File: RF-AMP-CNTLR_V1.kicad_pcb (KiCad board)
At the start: 4 copper layers, 220 x 100 mm, 384 parts, among them J101 VAC, J102 VDC, J103 ext_13V8, J104 Front Panel, J105 ANT_SWITCH, J106 BAND_SELECT, J107 I2C0, J108 VDD_IN, J109 VSS_IN, J110 RELAY RF OUT, J111 RELAY RF IN, J112 FWD3, J113 REF3, J114 FWD4, J115 REF4, J116 PTT, J117 ALC, J118 VDD_AMP, J119 GND_AMP, J120 SPI0, J121 I2C1, J122 RS232, J123 AMP1, J124 AMP2, J201 Raspberry_Pi_2_3, Q101 DTA124E, Q201 BSS138, Q202 BSS138, Q301 BC857, Q302 BC857, Q303 BC857, Q304 BC857, Q305 BC857, Q306 BC857, Q307 BC857, Q308 BC857, Q309 BC857, Q310 BC857, Q311 BC857, Q312 BC857, Q313 DTC124E, Q314 DTC124E, Q315 DTC124E, Q316 DTC124E, Q317 BC857, Q318 BC857, Q319 BC857, Q320 BC857, Q321 DTA124E, Q322 DTA124E, Q323 BC857, Q324 BC857, Q325 DTC124E, Q326 DTC124E, Q327 DTC124E, Q328 DTC124E, Q329 DTC124E, Q330 DTC124E, Q331 DTC124E, Q332 DTA124E, Q401 IXTH140P10T, Q402 IXTH140P10T, Q403 DTC124E, Q404 BC857, Q405 DTC124E, Q406 DTC124E, Q407 DTC124E, Q408 DTA124E, Q409 DTC124E, Q410 DTC124E, Q411 DTA124E, Q412 BCX53, Q413 DTA124E, Q414 DTC124E, Q415 DTC124E, Q416 BCX53, Q417 DTA124E, Q418 DTC124E, Q419 DTC124E, Q420 BCX53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

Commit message: Review
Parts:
- C102, C103: value 470n -> 68n
- C104, C110, C111, C112, C113, C120, C121, C122: value 100u -> 47u
- C108, C109: value 470n -> 47n
- C202: value 10u -> 47u
- D305, D306, D307, D308, D314, D315, D316, D317, D319, D404, D406, D409, D410, D413, D414: value DZ2S047X0L -> BZT52C4V7T-7
- D402: value DZ2S130X0L -> BZT52C13T-7
- D405: value DZ2S030X0L -> BZT52C13T-7
- F101, F102: value 0.1AT -> 1AT
- R406: value 10k -> 6k8
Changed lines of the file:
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@@
       (effects (font (size 1 1) (thickness 0.15)))
     )
-    (fp_text value 470n (at 5 3.25) (layer F.Fab)
+    (fp_text value 68n (at 5 3.25) (layer F.Fab)
       (effects (font (size 1 1) (thickness 0.15)))
     )
@@
       (effects (font (size 1 1) (thickness 0.15)))
     )
-    (fp_text value 470n (at 5 3.25) (layer F.Fab)
+    (fp_text value 68n (at 5 3.25) (layer F.Fab)
       (effects (font (size 1 1) (thickness 0.15)))
     )
@@
       (effects (font (size 1 1) (thickness 0.15)))
     )
-    (fp_text value 0.1AT (at 2.54 5 90) (layer F.Fab)
+    (fp_text value 1AT (at 2.54 5 90) (layer F.Fab)
       (effects (font (size 1 1) (thickness 0.15)))
     )
@@
       (effects (font (size 1 1) (thickness 0.15)))
     )
-    (fp_text value 0.1AT (at 2.54 5 90) (layer F.Fab)
+    (fp_text value 1AT (at 2.54 5 90) (layer F.Fab)
       (effects (font (size 1 1) (thickness 0.15)))
     )
@@
       (effects (font (size 1 1) (thickness 0.15)))
     )
-    (fp_text value 470n (at 2.5 3 90) (layer F.Fab)
+    (fp_text value 47n (at 2.5 3 90) (layer F.Fab)
       (effects (font (size 1 1) (thickness 0.15)))
     )
@@
       (effects (font (size 1 1) (thickness 0.15)))
     )
-    (fp_text value 470n (at 2.5 3 90) (layer F.Fab)
+    (fp_text value 47n (at 2.5 3 90) (layer F.Fab)
       (effects (font (size 1 1) (thickness 0.15)))
     )
@@
       (effects (font (size 1 1) (thickness 0.15)) (justify mirror))
     )
-    (fp_text value 100u (at 0 -2.55 90) (layer B.Fab)
+    (fp_text value 47u (at 0 -2.55 90) (layer B.Fab)
       (effects (font (size 1 1) (thickness 0.15)) (justify mirror))
     )
@@
       (effects (font (size 1 1) (thickness 0.15)) (justify mirror))
     )
-    (fp_text value 100u (at 0 -2.55 90) (layer B.Fab)
+    (fp_text value 47u (at 0 -2.55 90) (layer B.Fab)
       (effects (font (size 1 1) (thickness 0.15)) (justify mirror))
     )
@@
       (effects (font (size 1 1) (thickness 0.15)) (justify mirror))
     )
-    (fp_text value 100u (at 0 -2.55 270) (layer B.Fab)
+    (fp_text value 47u (at 0 -2.55 270) (layer B.Fab)
       (effects (font (size 1 1) (thickness 0.15)) (justify mirror))
     )
@@
       (effects (font (size 1 1) (thickness 0.15)) (justify mirror))
     )
-    (fp_text value 100u (at 0 -2.55 90) (layer B.Fab)
+    (fp_text value 47u (at 0 -2.55 90) (layer B.Fab)
       (effects (font (size 1 1) (thickness 0.15)) (justify mirror))
     )
@@
       (effects (font (size 1 1) (thickness 0.15)) (justify mirror))
     )
-    (fp_text value 100u (at 0 -2.55 90) (layer B.Fab)
+    (fp_text value 47u (at 0 -2.55 90) (layer B.Fab)
       (effects (font (size 1 1) (thickness 0.15)) (justify mirror))
     )
@@
       (effects (font (size 1 1) (thickness 0.15)) (justify mirror))
     )
-    (fp_text value 100u (at 0 -2.55 270) (layer B.Fab)
+    (fp_text value 47u (at 0 -2.55 270) (layer B.Fab)
       (effects (font (size 1 1) (thickness 0.15)) (justify mirror))
     )
@@
       (effects (font (size 1 1) (thickness 0.15)) (justify mirror))
     )
-    (fp_text value 100u (at 0 -2.55 90) (layer B.Fab)
+    (fp_text value 47u (at 0 -2.55 90) (layer B.Fab)
       (effects (font (size 1 1) (thickness 0.15)) (justify mirror))
     )
@@
       (effects (font (size 1 1) (thickness 0.15)) (justify mirror))
     )
-    (fp_text value 100u (at 0 -2.55 90) (layer B.Fab)
+    (fp_text value 47u (at 0 -2.55 90) (layer B.Fab)
       (effects (font (size 1 1) (thickness 0.15)) (justify mirror))
     )
@@
       (effects (font (size 1 1) (thickness 0.15)))
     )
-    (fp_text value 10u (at 0 2.55 270) (layer F.Fab)
+    (fp_text value 47u (at 0 2.55 270) (layer F.Fab)
       (effects (font (size 1 1) (thickness 0.15)))
     )
@@
       (effects (font (size 1 1) (thickness 0.15)) (justify mirror))
     )
-    (fp_text value DZ2S047X0L (at 0 -1.4) (layer B.Fab)
+    (fp_text value BZT52C4V7T-7 (at 0 -1.4) (layer B.Fab)
       (effects (font (size 1 1) (thickness 0.15)) (justify mirror))
     )
@@
       (effects (font (size 1 1) (thickness 0.15)) (justify mirror))
     )
-    (fp_text value DZ2S047X0L (at 0 -1.4) (layer B.Fab)
+    (fp_text value BZT52C4V7T-7 (at 0 -1.4) (layer B.Fab)
       (effects (font (size 1 1) (thickness 0.15)) (justify mirror))
     )
@@
       (effects (font (size 1 1) (thickness 0.15)) (justify mirror))
     )
-    (fp_text value DZ2S047X0L (at 0 -1.4 90) (layer B.Fab)
+    (fp_text value BZT52C4V7T-7 (at 0 -1.4 90) (layer B.Fab)
       (effects (font (size 1 1) (thickness 0.15)) (justify mirror))
     )
@@
       (effects (font (size 1 1) (thickness 0.15)) (justify mirror))
     )
-    (fp_text value DZ2S047X0L (at 0 -1.4) (layer B.Fab)
+    (fp_text value BZT52C4V7T-7 (at 0 -1.4) (layer B.Fab)
       (effects (font (size 1 1) (thickness 0.15)) (justify mirror))
     )
@@
       (effects (font (size 1 1) (thickness 0.15)))
     )
-    (fp_text value DZ2S047X0L (at 0 1.4) (layer F.Fab)
+    (fp_text value BZT52C4V7T-7 (at 0 1.4) (layer F.Fab)
       (effects (font (size 1 1) (thickness 0.15)))
     )
@@
       (effects (font (size 1 1) (thickness 0.15)))
     )
-    (fp_text value DZ2S047X0L (at 0 1.4) (layer F.Fab)
+    (fp_text value BZT52C4V7T-7 (at 0 1.4) (layer F.Fab)
       (effects (font (size 1 1) (thickness 0.15)))
     )
@@
       (effects (font (size 1 1) (thickness 0.15)))
     )
-    (fp_text value DZ2S047X0L (at 0 1.4) (layer F.Fab)
+    (fp_text value BZT52C4V7T-7 (at 0 1.4) (layer F.Fab)
       (effects (font (size 1 1) (thickness 0.15)))
     )
@@
       (effects (font (size 1 1) (thickness 0.15)))
     )
-    (fp_text value DZ2S047X0L (at 0 1.4) (layer F.Fab)
+    (fp_text value BZT52C4V7T-7 (at 0 1.4) (layer F.Fab)
       (effects (font (size 1 1) (thickness 0.15)))
     )
@@
       (effects (font (size 1 1) (thickness 0.15)))
     )
-    (fp_text value DZ2S047X0L (at 0 1.4 90) (layer F.Fab)
+    (fp_text value BZT52C4V7T-7 (at 0 1.4 90) (layer F.Fab)
       (effects (font (size 1 1) (thickness 0.15)))
     )
@@
       (effects (font (size 1 1) (thickness 0.15)))
     )
-    (fp_text value DZ2S130X0L (at 0 1.4 180) (layer F.Fab)
+    (fp_text value BZT52C13T-7 (at 0 1.4 180) (layer F.Fab)
       (effects (font (size 1 1) (thickness 0.15)))
     )
@@
       (effects (font (size 1 1) (thickness 0.15)))
     )
-    (fp_text value DZ2S047X0L (at 0 1.4 90) (layer F.Fab)
+    (fp_text value BZT52C4V7T-7 (at 0 1.4 90) (layer F.Fab)
       (effects (font (size 1 1) (thickness 0.15)))
     )
@@
       (effects (font (size 1 1) (thickness 0.15)))
     )
-    (fp_text value DZ2S030X0L (at 0 1.4 180) (layer F.Fab)
+    (fp_text value BZT52C13T-7 (at 0 1.4 180) (layer F.Fab)
       (effects (font (size 1 1) (thickness 0.15)))
     )
@@
       (effects (font (size 1 1) (thickness 0.15)))
     )
-    (fp_text value DZ2S047X0L (at 0 1.4 90) (layer F.Fab)
+    (fp_text value BZT52C4V7T-7 (at 0 1.4 90) (layer F.Fab)
       (effects (font (size 1 1) (thickness 0.15)))
     )
@@
       (effects (font (size 1 1) (thickness 0.15)))
     )
-    (fp_text value DZ2S047X0L (at 0 1.4) (layer F.Fab)
+    (fp_text value BZT52C4V7T-7 (at 0 1.4) (layer F.Fab)
       (effects (font (size 1 1) (thickness 0.15)))
     )
@@
       (effects (font (size 1 1) (thickness 0.15)))
     )
-    (fp_text value DZ2S047X0L (at 0 1.4) (layer F.Fab)
+    (fp_text value BZT52C4V7T-7 (at 0 1.4) (layer F.Fab)
       (effects (font (size 1 1) (thickness 0.15)))
     )
@@
       (effects (font (size 1 1) (thickness 0.15)))
     )
-    (fp_text value DZ2S047X0L (at 0 1.4 270) (layer F.Fab)
+    (fp_text value BZT52C4V7T-7 (at 0 1.4 270) (layer F.Fab)
       (effects (font (size 1 1) (thickness 0.15)))
     )
@@
       (effects (font (size 1 1) (thickness 0.15)))
     )
-    (fp_text value DZ2S047X0L (at 0 1.4) (layer F.Fab)
+    (fp_text value BZT52C4V7T-7 (at 0 1.4) (layer F.Fab)
       (effects (font (size 1 1) (thickness 0.15)))
     )
@@
       (effects (font (size 1 1) (thickness 0.15)) (justify mirror))
     )
-    (fp_text value 10k (at 0 -1.65) (layer B.Fab)
+    (fp_text value 6k8 (at 0 -1.65) (layer B.Fab)
       (effects (font (size 1 1) (thickness 0.15)) (justify mirror))
     )

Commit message: prototype bug fixes
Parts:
- C204: moved to B.Cu
- moved C204 40.6 mm to (104.6, 128.2), turned to 270 degrees
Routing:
- net Earth: track 213.5 -> 209.2 mm
- net Net-(C102-Pad1): track 43.0 -> 44.1 mm
- net Net-(C103-Pad2): track 108.5 -> 109.6 mm
- net Net-(C103-Pad1): track 94.7 -> 95.7 mm
- net Net-(C102-Pad2): track 34.8 -> 35.9 mm
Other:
- net class Vdd: clearance 1 -> 0.3
- board text added: "HB9GKW RF-AMP-CNTLR_V1"
- board text removed: "HB9GKW PA_CNTLR_V1"

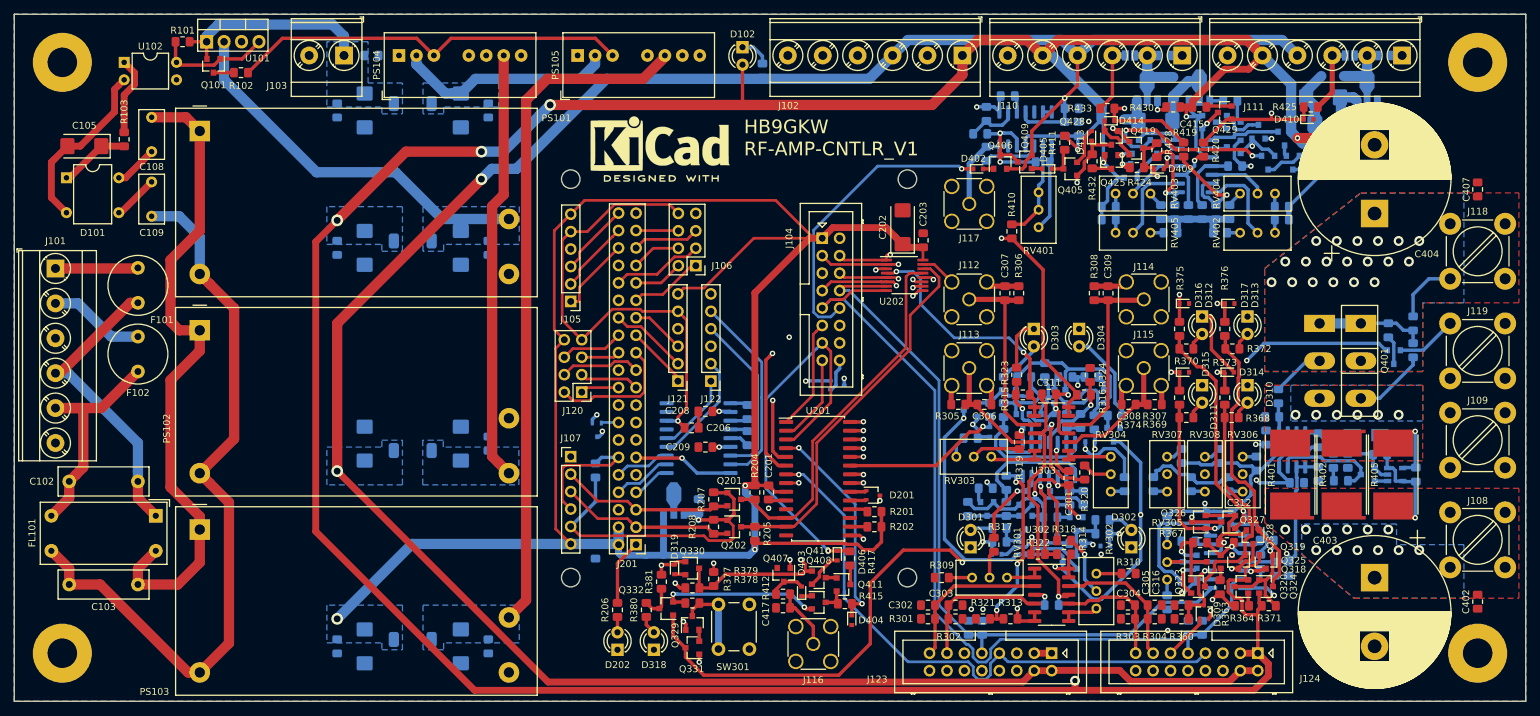
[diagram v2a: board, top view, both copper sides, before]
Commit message: new Version with AVR Controller
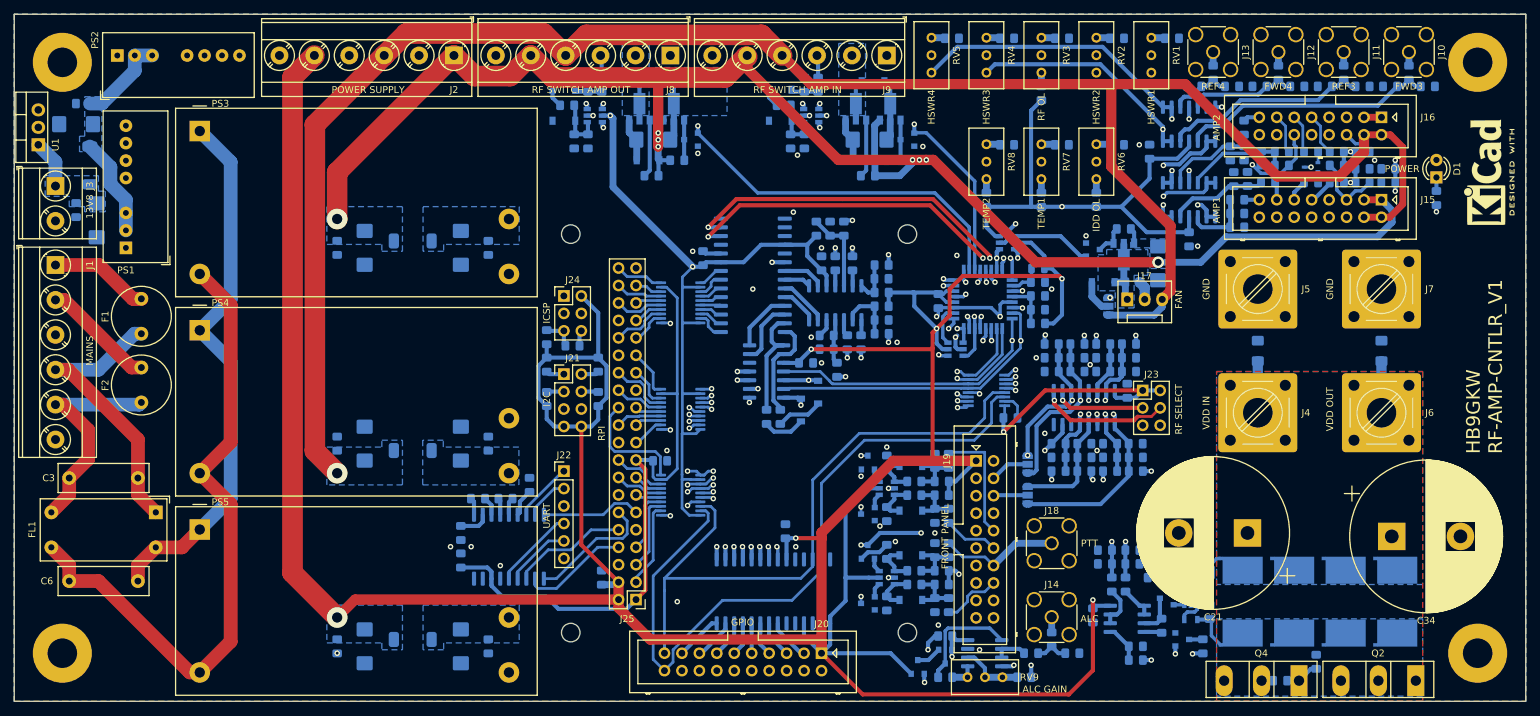
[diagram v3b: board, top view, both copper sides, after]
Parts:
- removed C101, C123, C201, C203, C204, C205, C206, C207, C208, C209, C301, C310, C311, C312, C401, C402, C405, C406, C407, C408, C409, C410, C411, C412, C413, C414, C415, C416, C417, C418, C419, C423, C427: 100n, Capacitor_SMD:C_0805_2012Metric_Pad1.15x1.40mm_HandSolder
- removed C105, C202: 47u, Capacitor_Tantalum_SMD:CP_EIA-6032-28_Kemet-C
- removed C108, C109: 47n, Capacitor_THT:C_Rect_L7.0mm_W3.5mm_P5.00mm
- removed C302, C303, C304, C305, C306, C307, C308, C309, C313, C314, C315, C316: 47n, Capacitor_SMD:C_0805_2012Metric_Pad1.15x1.40mm_HandSolder
- removed C403, C404: 470u, Capacitor_THT:CP_Radial_D22.0mm_P10.00mm_SnapIn
- removed C420, C421, C424, C425: 1u, Capacitor_SMD:C_0805_2012Metric_Pad1.15x1.40mm_HandSolder
- removed C422, C426: 4u7, Capacitor_Tantalum_SMD:CP_EIA-6032-28_Kemet-C
- removed D101: B80C800DM, Diode_THT:Diode_Bridge_DIP-4_W7.62mm_P5.08mm
- removed D103, D104, D309: BAT54CW, Package_TO_SOT_SMD:SOT-323_SC-70
- removed D201: BAT54AW, Package_TO_SOT_SMD:SOT-323_SC-70
- removed D202: RP_ON, LED_THT:LED_D3.0mm
- removed D301: HSWR1, LED_THT:LED_D3.0mm
- removed D302: HSWR2, LED_THT:LED_D3.0mm
- removed D303: HSWR3, LED_THT:LED_D3.0mm
- removed D304: HSWR4, LED_THT:LED_D3.0mm
- removed D305, D306, D307, D308, D314, D315, D316, D317, D319, D404, D406, D409, D410, D413, D414: BZT52C4V7T-7, Diode_SMD:D_SOD-523
- removed D310: RF_OL, LED_THT:LED_D3.0mm
- removed D311: TEMP1, LED_THT:LED_D3.0mm
- removed D312: TEMP2, LED_THT:LED_D3.0mm
- removed D313: OC, LED_THT:LED_D3.0mm
- removed D318: FAULT, LED_THT:LED_D3.0mm
- removed D401: Z1SMA33, Diode_SMD:D_SMA
- removed D402, D405: BZT52C13T-7, Diode_SMD:D_SOD-523
- removed D403: DZ2S047X0L, Diode_SMD:D_SOD-523
- removed D407, D408, D411, D412: PMEG6010CEH, Diode_SMD:D_SOD-123
- removed J104: Front Panel, Connector_Multicomp:Multicomp_MC9A12-1634_2x08_P2.54mm_Vertical
- removed J105: ANT_SWITCH, Connector_PinHeader_2.54mm:PinHeader_1x06_P2.54mm_Vertical
- removed J106: BAND_SELECT, Connector_PinHeader_2.54mm:PinHeader_2x04_P2.54mm_Vertical
- removed J107: I2C0, Connector_PinHeader_2.54mm:PinHeader_1x06_P2.54mm_Vertical
- removed J108: VDD_IN, TerminalBlock_MetzConnect:TerminalBlock_MetzConnect_360425_1x01_Horizontal_ScrewM4.0_Boxed
- removed J109: VSS_IN, TerminalBlock_MetzConnect:TerminalBlock_MetzConnect_360425_1x01_Horizontal_ScrewM4.0_Boxed
- removed J112: FWD3, Connector_Coaxial:SMA_Amphenol_132134_Vertical
- removed J113: REF3, Connector_Coaxial:SMA_Amphenol_132134_Vertical
- removed J114: FWD4, Connector_Coaxial:SMA_Amphenol_132134_Vertical
- removed J115: REF4, Connector_Coaxial:SMA_Amphenol_132134_Vertical
- removed J116: PTT, Connector_Coaxial:SMA_Amphenol_132134_Vertical
- removed J117: ALC, Connector_Coaxial:SMA_Amphenol_132134_Vertical
- removed J118: VDD_AMP, TerminalBlock_MetzConnect:TerminalBlock_MetzConnect_360425_1x01_Horizontal_ScrewM4.0_Boxed
- removed J119: GND_AMP, TerminalBlock_MetzConnect:TerminalBlock_MetzConnect_360425_1x01_Horizontal_ScrewM4.0_Boxed
- removed J120: SPI0, Connector_PinHeader_2.54mm:PinHeader_2x04_P2.54mm_Vertical
- removed J121: I2C1, Connector_PinHeader_2.54mm:PinHeader_1x06_P2.54mm_Vertical
- removed J122: RS232, Connector_PinHeader_2.54mm:PinHeader_1x06_P2.54mm_Vertical
- removed J123: AMP1, Connector_Multicomp:Multicomp_MC9A12-1634_2x08_P2.54mm_Vertical
- removed J124: AMP2, Connector_Multicomp:Multicomp_MC9A12-1634_2x08_P2.54mm_Vertical
- removed JP401, JP402: SolderJumper_2_Open, Jumper:SolderJumper-2_P1.3mm_Open_Pad1.0x1.5mm
- removed Q101, Q321, Q322, Q332, Q408, Q411, Q413, Q417, Q421, Q425: DTA124E, Package_TO_SOT_SMD:SOT-23
- removed Q201, Q202: BSS138, Package_TO_SOT_SMD:SOT-23
- removed Q301, Q302, Q303, Q304, Q305, Q306, Q307, Q308, Q309, Q310, Q311, Q312, Q317, Q318, Q319, Q320, Q323, Q324, Q404: BC857, Package_TO_SOT_SMD:SOT-23
- removed Q313, Q314, Q315, Q316, Q325, Q326, Q327, Q328, Q329, Q330, Q331, Q403, Q405, Q406, Q407, Q409, Q410, Q414, Q415, Q418, Q419, Q422, Q423, Q424, Q427, Q428, Q429: DTC124E, Package_TO_SOT_SMD:SOT-23
- removed Q401, Q402: IXTH140P10T, Package_TO_SOT_THT:TO-247-3_Vertical
- removed Q412, Q416, Q420, Q426: BCX53, Package_TO_SOT_SMD:SOT-89-3
- removed R101, R325, R326, R327, R328, R333, R334, R335, R336, R363, R364, R365, R366, R378: 22k, Resistor_SMD:R_0805_2012Metric_Pad1.15x1.40mm_HandSolder
- removed R102, R377, R412, R415, R417, R424, R425, R432, R433, R434, R435, R436, R437: 1k, Resistor_SMD:R_0805_2012Metric_Pad1.15x1.40mm_HandSolder
- removed R103: 620, Resistor_SMD:R_0805_2012Metric_Pad1.15x1.40mm_HandSolder
- removed R104, R201, R202: 2k2, Resistor_SMD:R_0805_2012Metric_Pad1.15x1.40mm_HandSolder
- removed R203: 1k5, Resistor_SMD:R_0805_2012Metric_Pad1.15x1.40mm_HandSolder
- removed R204, R205, R206: 2k7, Resistor_SMD:R_0805_2012Metric_Pad1.15x1.40mm_HandSolder
- removed R207, R208: 1k8, Resistor_SMD:R_0805_2012Metric_Pad1.15x1.40mm_HandSolder
- removed R301, R302, R303, R304, R305, R306, R307, R308, R353, R356, R359, R360, R361, R362, R403, R409, R414: 100k, Resistor_SMD:R_0805_2012Metric_Pad1.15x1.40mm_HandSolder
- removed R309, R310, R311, R312, R350, R352: 15k, Resistor_SMD:R_0805_2012Metric_Pad1.15x1.40mm_HandSolder
- removed R313, R314, R315, R316: 82k, Resistor_SMD:R_0805_2012Metric_Pad1.15x1.40mm_HandSolder
- removed R317, R318, R319, R320, R349, R351, R354, R357, R379, R411, R418, R421, R426, R429: 47k, Resistor_SMD:R_0805_2012Metric_Pad1.15x1.40mm_HandSolder
- removed R321, R322, R323, R324, R337, R339, R341, R343, R355, R358, R367, R371, R404, R410, R413, R419, R420, R422, R423, R427, R428, R430, R431: 10k, Resistor_SMD:R_0805_2012Metric_Pad1.15x1.40mm_HandSolder
- removed R329, R330, R331, R332: 820k, Resistor_SMD:R_0805_2012Metric_Pad1.15x1.40mm_HandSolder
- removed R338, R340, R342, R344, R368, R369, R370, R372, R380, R407: 4k7, Resistor_SMD:R_0805_2012Metric_Pad1.15x1.40mm_HandSolder
- removed R345, R346, R347, R348, R373, R374, R375, R376, R381: 470, Resistor_SMD:R_0805_2012Metric_Pad1.15x1.40mm_HandSolder
- removed R401, R402, R405: 0R015, Resistor_SMD:R_Shunt_Vishay_WSR2_WSR3_KelvinConnection
- removed R406: 6k8, Resistor_SMD:R_0805_2012Metric_Pad1.15x1.40mm_HandSolder
- removed R408: 68k, Resistor_SMD:R_0805_2012Metric_Pad1.15x1.40mm_HandSolder
- removed R416: 33k, Resistor_SMD:R_0805_2012Metric_Pad1.15x1.40mm_HandSolder
- removed the REF** at (114.0, 68.8)
- removed RV301, RV302, RV303, RV304, RV305, RV306, RV307, RV308: 50k, Potentiometer_THT:Potentiometer_Bourns_3296W_Vertical
- removed RV401, RV402, RV403, RV404, RV405: 20k, Potentiometer_THT:Potentiometer_Bourns_3296W_Vertical
- removed SW301: RESET, Button_Switch_THT:SW_PUSH_6mm
- removed U101: KA378R12C, Package_TO_SOT_THT:TO-220-4_Vertical
- removed U102: SFH617A-2, Package_DIP:DIP-4_W7.62mm
- removed U103: L78L33_SOT89, Package_TO_SOT_SMD:SOT-89-3
- removed U201: MCP23017_SO, Package_SO:SOIC-28W_7.5x17.9mm_P1.27mm
- removed U202: MAX11616, Package_SO:QSOP-16_3.9x4.9mm_P0.635mm
- removed U203: MAX3232, Package_SO:SOIC-18W_7.5x11.6mm_P1.27mm
- removed U301, U304, U404: LM339, Package_SO:SOIC-14_3.9x8.7mm_P1.27mm
- removed U302, U303, U402: MC33079, Package_SO:SOIC-14_3.9x8.7mm_P1.27mm
- removed U401: MC33078, Package_SO:SOIC-8_3.9x4.9mm_P1.27mm
- removed U403: INA138, Package_TO_SOT_SMD:SOT-23-5
- added C19: 100n, Capacitor_SMD:C_0805_2012Metric_Pad1.15x1.40mm_HandSolder, B.Cu at (177.0, 137.5)
- added C20: 100n, Capacitor_SMD:C_1206_3216Metric_Pad1.42x1.75mm_HandSolder, B.Cu at (201.0, 99.0)
- added C21: 470u, Capacitor_THT:CP_Radial_D22.0mm_P10.00mm_SnapIn, F.Cu at (199.5, 125.5)
- added C22: 47n, Capacitor_SMD:C_0805_2012Metric_Pad1.15x1.40mm_HandSolder, B.Cu at (199.5, 74.0)
- added C23: 47n, Capacitor_SMD:C_0805_2012Metric_Pad1.15x1.40mm_HandSolder, B.Cu at (198.0, 79.0)
- added C24: 47n, Capacitor_SMD:C_0805_2012Metric_Pad1.15x1.40mm_HandSolder, B.Cu at (201.5, 71.0)
- added C25: 47n, Capacitor_SMD:C_0805_2012Metric_Pad1.15x1.40mm_HandSolder, B.Cu at (199.0, 70.2)
- added C26: 100n, Capacitor_SMD:C_0805_2012Metric_Pad1.15x1.40mm_HandSolder, B.Cu at (194.0, 137.0)
- added C27: 47n, Capacitor_SMD:C_0805_2012Metric_Pad1.15x1.40mm_HandSolder, B.Cu at (174.8, 100.0)
- added C28: 47n, Capacitor_SMD:C_0805_2012Metric_Pad1.15x1.40mm_HandSolder, B.Cu at (183.2, 114.5)
- added C29: 47n, Capacitor_SMD:C_0805_2012Metric_Pad1.15x1.40mm_HandSolder, B.Cu at (178.5, 100.0)
- added C30: 47n, Capacitor_SMD:C_0805_2012Metric_Pad1.15x1.40mm_HandSolder, B.Cu at (172.0, 114.5)
- added C31: 100n, Capacitor_SMD:C_0805_2012Metric_Pad1.15x1.40mm_HandSolder, B.Cu at (192.2, 134.0)
- added C32: 100n, Capacitor_SMD:C_0805_2012Metric_Pad1.15x1.40mm_HandSolder, B.Cu at (182.8, 130.0)
- added C33: 100n, Capacitor_SMD:C_0805_2012Metric_Pad1.15x1.40mm_HandSolder, B.Cu at (204.2, 147.0)
- added C34: 470u, Capacitor_THT:CP_Radial_D22.0mm_P10.00mm_SnapIn, F.Cu at (220.5, 126.0)
- added C35: 100n, Capacitor_SMD:C_1206_3216Metric_Pad1.42x1.75mm_HandSolder, B.Cu at (219.0, 99.0)
- added C36: 100n, Capacitor_SMD:C_0805_2012Metric_Pad1.15x1.40mm_HandSolder, B.Cu at (178.8, 130.0)
- added C37: 47n, Capacitor_SMD:C_0805_2012Metric_Pad1.15x1.40mm_HandSolder, B.Cu at (220.2, 60.5)
- added C38: 47n, Capacitor_SMD:C_0805_2012Metric_Pad1.15x1.40mm_HandSolder, B.Cu at (210.8, 60.5)
- added C39: 47n, Capacitor_SMD:C_0805_2012Metric_Pad1.15x1.40mm_HandSolder, B.Cu at (201.2, 60.5)
- added C40: 47n, Capacitor_SMD:C_0805_2012Metric_Pad1.15x1.40mm_HandSolder, B.Cu at (191.8, 60.5)
- added C41: 47n, Capacitor_SMD:C_0805_2012Metric_Pad1.15x1.40mm_HandSolder, B.Cu at (182.2, 100.0)
- added C42: 47n, Capacitor_SMD:C_0805_2012Metric_Pad1.15x1.40mm_HandSolder, B.Cu at (179.5, 114.5)
- added C43: 47n, Capacitor_SMD:C_0805_2012Metric_Pad1.15x1.40mm_HandSolder, B.Cu at (171.0, 100.0)
- added C44: 47n, Capacitor_SMD:C_0805_2012Metric_Pad1.15x1.40mm_HandSolder, B.Cu at (175.8, 112.5)
- added C45: 100n, Capacitor_SMD:C_0805_2012Metric_Pad1.15x1.40mm_HandSolder, B.Cu at (155.5, 140.5)
- added C46: 47n, Capacitor_SMD:C_0805_2012Metric_Pad1.15x1.40mm_HandSolder, B.Cu at (216.2, 74.5)
- added C47: 47n, Capacitor_SMD:C_0805_2012Metric_Pad1.15x1.40mm_HandSolder, B.Cu at (216.2, 70.0)
- added C48: 47n, Capacitor_SMD:C_0805_2012Metric_Pad1.15x1.40mm_HandSolder, B.Cu at (220.0, 74.5)
- added C49: 100n, Capacitor_SMD:C_0805_2012Metric_Pad1.15x1.40mm_HandSolder, B.Cu at (174.0, 143.0)
- added C50: 100n, Capacitor_SMD:C_0805_2012Metric_Pad1.15x1.40mm_HandSolder, B.Cu at (137.5, 86.2)
- added C51: 100n, Capacitor_SMD:C_0805_2012Metric_Pad1.15x1.40mm_HandSolder, B.Cu at (191.0, 82.8)
- added C52: 100n, Capacitor_SMD:C_0805_2012Metric_Pad1.15x1.40mm_HandSolder, B.Cu at (135.2, 100.8)
- added C53: 100n, Capacitor_SMD:C_0805_2012Metric_Pad1.15x1.40mm_HandSolder, B.Cu at (185.2, 70.0)
- added C54: 4u7, Capacitor_Tantalum_SMD:CP_EIA-6032-28_Kemet-C, B.Cu at (113.0, 68.2)
- added C55: 4u7, Capacitor_Tantalum_SMD:CP_EIA-6032-28_Kemet-C, B.Cu at (144.5, 68.2)
- added C56: 47n, Capacitor_SMD:C_0805_2012Metric_Pad1.15x1.40mm_HandSolder, B.Cu at (103.5, 60.2)
- added C57: 47n, Capacitor_SMD:C_0805_2012Metric_Pad1.15x1.40mm_HandSolder, B.Cu at (103.5, 68.5)
- added C58: 47n, Capacitor_SMD:C_0805_2012Metric_Pad1.15x1.40mm_HandSolder, B.Cu at (135.0, 60.2)
- added C59: 47n, Capacitor_SMD:C_0805_2012Metric_Pad1.15x1.40mm_HandSolder, B.Cu at (133.0, 68.5)
- added C60: 1n, Capacitor_SMD:C_0805_2012Metric_Pad1.15x1.40mm_HandSolder, B.Cu at (154.0, 128.0)
- added C61: 1n, Capacitor_SMD:C_0805_2012Metric_Pad1.15x1.40mm_HandSolder, B.Cu at (154.0, 136.0)
- added C62: 1n, Capacitor_SMD:C_0805_2012Metric_Pad1.15x1.40mm_HandSolder, B.Cu at (154.0, 115.0)
- added C63: 1n, Capacitor_SMD:C_0805_2012Metric_Pad1.15x1.40mm_HandSolder, B.Cu at (154.0, 123.0)
- added C64: 100n, Capacitor_SMD:C_0805_2012Metric_Pad1.15x1.40mm_HandSolder, B.Cu at (182.0, 104.8)
- added C65: 100n, Capacitor_SMD:C_0805_2012Metric_Pad1.15x1.40mm_HandSolder, B.Cu at (147.0, 128.2)
- added C66: 100n, Capacitor_SMD:C_0805_2012Metric_Pad1.15x1.40mm_HandSolder, B.Cu at (147.0, 135.8)
- added C67: 100n, Capacitor_SMD:C_0805_2012Metric_Pad1.15x1.40mm_HandSolder, B.Cu at (147.0, 115.2)
- added C68: 100n, Capacitor_SMD:C_0805_2012Metric_Pad1.15x1.40mm_HandSolder, B.Cu at (147.0, 122.8)
- added C69: 1n, Capacitor_SMD:C_0805_2012Metric_Pad1.15x1.40mm_HandSolder, B.Cu at (101.2, 98.2)
- added C70: 100n, Capacitor_SMD:C_0805_2012Metric_Pad1.15x1.40mm_HandSolder, B.Cu at (169.0, 91.0)
- added C71: 100n, Capacitor_SMD:C_0805_2012Metric_Pad1.15x1.40mm_HandSolder, B.Cu at (154.5, 91.8)
- added C72: 100n, Capacitor_SMD:C_0805_2012Metric_Pad1.15x1.40mm_HandSolder, B.Cu at (169.0, 89.0)
- added C73: 1n, Capacitor_SMD:C_0805_2012Metric_Pad1.15x1.40mm_HandSolder, B.Cu at (182.8, 89.0)
- added C74: 47u, Capacitor_Tantalum_SMD:CP_EIA-6032-28_Kemet-C, B.Cu at (186.5, 86.2)
- added C75: 100n, Capacitor_SMD:C_0805_2012Metric_Pad1.15x1.40mm_HandSolder, B.Cu at (120.2, 85.5)
- added C76: 100n, Capacitor_SMD:C_0805_2012Metric_Pad1.15x1.40mm_HandSolder, B.Cu at (165.0, 108.8)
- added C77: 100n, Capacitor_SMD:C_0805_2012Metric_Pad1.15x1.40mm_HandSolder, B.Cu at (87.5, 120.5)
- added C78: 100n, Capacitor_SMD:C_0805_2012Metric_Pad1.15x1.40mm_HandSolder, B.Cu at (114.0, 115.0)
- added C79: 100n, Capacitor_SMD:C_0805_2012Metric_Pad1.15x1.40mm_HandSolder, B.Cu at (105.5, 132.0)
- added C80: 100n, Capacitor_SMD:C_0805_2012Metric_Pad1.15x1.40mm_HandSolder, B.Cu at (132.2, 125.2)
- added C81: 100n, Capacitor_SMD:C_0805_2012Metric_Pad1.15x1.40mm_HandSolder, B.Cu at (85.0, 129.5)
- added C82: 100n, Capacitor_SMD:C_0805_2012Metric_Pad1.15x1.40mm_HandSolder, B.Cu at (91.5, 120.5)
- added C83: 100n, Capacitor_SMD:C_0805_2012Metric_Pad1.15x1.40mm_HandSolder, B.Cu at (85.0, 125.5)
- added C84: 100n, Capacitor_SMD:C_0805_2012Metric_Pad1.15x1.40mm_HandSolder, B.Cu at (95.0, 118.5)
- added D10: 1N4148W, Diode_SMD:D_SOD-123, B.Cu at (100.0, 61.0)
- added D11: 1N4148W, Diode_SMD:D_SOD-123, B.Cu at (131.5, 61.0)
- added D12: PMEG6010CEH, Diode_SMD:D_SOD-123, B.Cu at (112.2, 71.2)
- added D13: PMEG6010CEH, Diode_SMD:D_SOD-123, B.Cu at (143.8, 71.2)
- added D14: 1N4148W, Diode_SMD:D_SOD-123, B.Cu at (150.5, 128.8)
- added D15: 1N4148W, Diode_SMD:D_SOD-123, B.Cu at (150.5, 135.2)
- added D16: 1N4148W, Diode_SMD:D_SOD-123, B.Cu at (150.5, 115.8)
- added D17: 1N4148W, Diode_SMD:D_SOD-123, B.Cu at (150.5, 122.2)
- added D18: PMEG6010CEH, Diode_SMD:D_SOD-123, B.Cu at (178.5, 89.0)
- added D2: Z1SMA33, Diode_SMD:D_SMA, B.Cu at (191.5, 131.2)
- added D3: 1N4148W, Diode_SMD:D_SOD-123, B.Cu at (134.5, 107.6)
- added D4: BAT54CW, Package_TO_SOT_SMD:SOT-323_SC-70, B.Cu at (208.8, 72.2)
- added D5: 1N4148W, Diode_SMD:D_SOD-123, B.Cu at (137.0, 105.0)
- added D6: PMEG6010CEH, Diode_SMD:D_SOD-123, B.Cu at (113.5, 59.8)
- added D7: BZT52C4V7T-7, Diode_SMD:D_SOD-123, B.Cu at (100.0, 65.5)
- added D8: PMEG6010CEH, Diode_SMD:D_SOD-123, B.Cu at (145.0, 59.8)
- added D9: BZT52C4V7T-7, Diode_SMD:D_SOD-123, B.Cu at (131.5, 65.5)
- added FB1: Ferrite_Bead_Small, Resistor_SMD:R_0805_2012Metric_Pad1.15x1.40mm_HandSolder, B.Cu at (202.5, 74.5)
- added FB10: Ferrite_Bead_Small, Resistor_SMD:R_0805_2012Metric_Pad1.15x1.40mm_HandSolder, B.Cu at (212.5, 70.0)
- added FB11: Ferrite_Bead_Small, Resistor_SMD:R_0805_2012Metric_Pad1.15x1.40mm_HandSolder, B.Cu at (208.8, 74.5)
- added FB12: Ferrite_Bead_Small, Resistor_SMD:R_0805_2012Metric_Pad1.15x1.40mm_HandSolder, B.Cu at (208.8, 70.0)
- added FB13: Ferrite_Bead_Small, Resistor_SMD:R_0805_2012Metric_Pad1.15x1.40mm_HandSolder, B.Cu at (171.0, 141.0)
- added FB14: Ferrite_Bead_Small, Resistor_SMD:R_0805_2012Metric_Pad1.15x1.40mm_HandSolder, B.Cu at (105.5, 60.2)
- added FB15: Ferrite_Bead_Small, Resistor_SMD:R_0805_2012Metric_Pad1.15x1.40mm_HandSolder, B.Cu at (137.0, 60.2)
- added FB16: Ferrite_Bead_Small, Resistor_SMD:R_0805_2012Metric_Pad1.15x1.40mm_HandSolder, B.Cu at (156.0, 128.0)
- added FB17: Ferrite_Bead_Small, Resistor_SMD:R_0805_2012Metric_Pad1.15x1.40mm_HandSolder, B.Cu at (156.0, 136.0)
- added FB18: Ferrite_Bead_Small, Resistor_SMD:R_0805_2012Metric_Pad1.15x1.40mm_HandSolder, B.Cu at (156.0, 115.0)
- added FB19: Ferrite_Bead_Small, Resistor_SMD:R_0805_2012Metric_Pad1.15x1.40mm_HandSolder, B.Cu at (156.0, 123.0)
- added FB2: Ferrite_Bead_Small, Resistor_SMD:R_0805_2012Metric_Pad1.15x1.40mm_HandSolder, B.Cu at (198.0, 77.0)
- added FB3: Ferrite_Bead_Small, Resistor_SMD:R_0805_2012Metric_Pad1.15x1.40mm_HandSolder, B.Cu at (204.5, 70.0)
- added FB4: Ferrite_Bead_Small, Resistor_SMD:R_0805_2012Metric_Pad1.15x1.40mm_HandSolder, B.Cu at (199.0, 66.5)
- added FB5: Ferrite_Bead_Small, Resistor_SMD:R_0805_2012Metric_Pad1.15x1.40mm_HandSolder, B.Cu at (223.0, 58.5)
- added FB6: Ferrite_Bead_Small, Resistor_SMD:R_0805_2012Metric_Pad1.15x1.40mm_HandSolder, B.Cu at (213.5, 58.5)
- added FB7: Ferrite_Bead_Small, Resistor_SMD:R_0805_2012Metric_Pad1.15x1.40mm_HandSolder, B.Cu at (204.0, 58.5)
- added FB8: Ferrite_Bead_Small, Resistor_SMD:R_0805_2012Metric_Pad1.15x1.40mm_HandSolder, B.Cu at (194.5, 58.5)
- added FB9: Ferrite_Bead_Small, Resistor_SMD:R_0805_2012Metric_Pad1.15x1.40mm_HandSolder, B.Cu at (212.5, 74.5)
- added J10: FWD3, Connector_Coaxial:SMA_Amphenol_132134_Vertical, F.Cu at (223.0, 55.5)
- added J11: REF3, Connector_Coaxial:SMA_Amphenol_132134_Vertical, F.Cu at (213.5, 55.5)
- added J12: FWD4, Connector_Coaxial:SMA_Amphenol_132134_Vertical, F.Cu at (204.0, 55.5)
- added J13: REF4, Connector_Coaxial:SMA_Amphenol_132134_Vertical, F.Cu at (194.5, 55.5)
- added J14: ALC, Connector_Coaxial:SMA_Amphenol_132134_Vertical, F.Cu at (171.0, 137.8)
- added J15: AMP1, Connector_Multicomp:Multicomp_MC9A12-1634_2x08_P2.54mm_Vertical, F.Cu at (219.0, 77.0)
- added J16: AMP2, Connector_Multicomp:Multicomp_MC9A12-1634_2x08_P2.54mm_Vertical, F.Cu at (219.0, 65.0)
- added J17: FAN, Connector:FanPinHeader_1x03_P2.54mm_Vertical, F.Cu at (182.0, 91.5)
- added J18: PTT, Connector_Coaxial:SMA_Amphenol_132134_Vertical, F.Cu at (171.0, 127.0)
- added J19: FRONT PANEL, Connector_Multicomp:Multicomp_MC9A12-2034_2x10_P2.54mm_Vertical, F.Cu at (160.0, 115.0)
- added J20: GPIO, Connector_Multicomp:Multicomp_MC9A12-2034_2x10_P2.54mm_Vertical, F.Cu at (137.5, 143.0)
- added J21: I2C, Connector_PinHeader_2.54mm:PinHeader_2x04_P2.54mm_Vertical, F.Cu at (100.0, 102.4)
- added J22: UART, Connector_PinHeader_2.54mm:PinHeader_1x06_P2.54mm_Vertical, F.Cu at (100.0, 116.5)
- added J23: Conn_02x03_Odd_Even, Connector_PinHeader_2.54mm:PinHeader_2x03_P2.54mm_Vertical, F.Cu at (184.2, 104.8)
- added J24: ICSP, Connector_PinHeader_2.54mm:PinHeader_2x03_P2.54mm_Vertical, F.Cu at (100.0, 91.0)
- added J4: VDD IN, footprints-cache:TerminalBlock_MetzConnect_360425_1x01_Horizontal_ScrewM4.0_Boxed, F.Cu at (197.0, 104.0)
- added J5: VSS IN, footprints-cache:TerminalBlock_MetzConnect_360425_1x01_Horizontal_ScrewM4.0_Boxed, F.Cu at (197.0, 86.0)
- added J6: VDD OUT, footprints-cache:TerminalBlock_MetzConnect_360425_1x01_Horizontal_ScrewM4.0_Boxed, F.Cu at (215.0, 104.0)
- added J7: VSS OUT, footprints-cache:TerminalBlock_MetzConnect_360425_1x01_Horizontal_ScrewM4.0_Boxed, F.Cu at (215.0, 86.0)
- added JP1: SolderJumper_3_Bridged12, Jumper:SolderJumper-3_P1.3mm_Open_RoundedPad1.0x1.5mm, B.Cu at (167.5, 115.5)
- added JP2: SolderJumper_3_Bridged12, Jumper:SolderJumper-3_P1.3mm_Open_RoundedPad1.0x1.5mm, B.Cu at (167.5, 120.0)
- added JP3: SolderJumper_3_Bridged12, Jumper:SolderJumper-3_P1.3mm_Open_RoundedPad1.0x1.5mm, B.Cu at (179.2, 92.5)
- added L5: 10u, Inductor_SMD:L_0805_2012Metric, B.Cu at (169.0, 87.0)
- added Q1: BC857, Package_TO_SOT_SMD:SOT-23, B.Cu at (187.8, 135.0)
- added Q10: BCX53, Package_TO_SOT_SMD:SOT-89-3, B.Cu at (147.5, 63.8)
- added Q11: BCX53, Package_TO_SOT_SMD:SOT-89-3, B.Cu at (111.0, 63.8)
- added Q12: BCX53, Package_TO_SOT_SMD:SOT-89-3, B.Cu at (142.5, 63.8)
- added Q13: DTC124E, Package_TO_SOT_SMD:SOT-23, B.Cu at (144.2, 128.2)
- added Q14: DTC124E, Package_TO_SOT_SMD:SOT-23, B.Cu at (144.2, 135.8)
- added Q15: DTC124E, Package_TO_SOT_SMD:SOT-23, B.Cu at (144.2, 115.2)
- added Q16: DTC124E, Package_TO_SOT_SMD:SOT-23, B.Cu at (144.2, 122.8)
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- renumbered C104 to C1, C114 to C10, C115 to C11, C116 to C12, C117 to C13, C118 to C14, C119 to C15, C120 to C16, C121 to C17, C122 to C18, C106 to C2, C102 to C3, C107 to C4, C110 to C5, C103 to C6, C111 to C7, C112 to C8, C113 to C9, D102 to D1, F101 to F1, F102 to F2, FL101 to FL1, J101 to J1, J102 to J2, J201 to J25, J103 to J3, L101 to L1, L102 to L2, L103 to L3, L104 to L4, PS104 to PS1, PS105 to PS2, PS101 to PS3, PS102 to PS4, PS103 to PS5
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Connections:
- net +12V_ renamed /+12V_
- net +5V_ renamed /+5V_
- net -12V_ renamed /-12V_
- C4 pad 1: Net-(C107-Pad1) -> Net-(C4-Pad1)
- C5 pad 1: Net-(C107-Pad1) -> Net-(C4-Pad1)
- J25 pad 1: Net-(J201-Pad1) -> +3V3
- J25 pad 12: /CONTROLLER/INT_OC -> /CONTROLLER/TXD1
- J25 pad 13: PTT_DIG -> /CONTROLLER/ON_AIR_LV
- J25 pad 15: ILK_CMD_PI -> /CONTROLLER/RF_SW2_ON_LV
- J25 pad 16: RESET_CMD_PI -> /CONTROLLER/GATE_ALC_EN_LV
- J25 pad 17: Net-(J201-Pad17) -> +3V3
- J25 pad 18: OP_CMD_PI -> /CONTROLLER/RF_SW1_ON_LV
- J25 pad 19: /CONTROLLER/MOSI0 -> /CONTROLLER/MOSI_FAN_LV
- J25 pad 21: /CONTROLLER/MISO0 -> /CONTROLLER/MISO_RF_INHIBIT_LV
- J25 pad 22: FAULT -> /CONTROLLER/RESET_ISP_LV
- J25 pad 23: /CONTROLLER/SCLK0 -> /CONTROLLER/SCK_SOFT_ILK_LV
- J25 pad 24: /CONTROLLER/CE0 -> /CONTROLLER/VDD_EN_LV
- J25 pad 26: /CONTROLLER/CE1 -> /CONTROLLER/OPR_LV
- J25 pad 27: /CONTROLLER/SDA1_LV -> /CONTROLLER/DISPLAY_LV
- J25 pad 28: /CONTROLLER/SCL1_LV -> /CONTROLLER/PTT_LV
- J25 pad 29: /CONTROLLER/BAND1 -> /CONTROLLER/RESET_ILK_LV
- J25 pad 3: /CONTROLLER/SDA0_LV -> /CONTROLLER/SDA_PI_LV
- J25 pad 31: /CONTROLLER/BAND2 -> /CONTROLLER/HSWR1_LV
- J25 pad 32: /CONTROLLER/BAND3 -> /CONTROLLER/HSWR2_LV
- J25 pad 33: /CONTROLLER/BAND4 -> /CONTROLLER/HSWR3_LV
- J25 pad 35: /CONTROLLER/BAND5 -> /CONTROLLER/RF_OL_LV
- J25 pad 36: /CONTROLLER/ANT1 -> /CONTROLLER/UNBAL_LV
- J25 pad 37: /CONTROLLER/BAND6 -> /CONTROLLER/VDD_LIM_LV
- J25 pad 38: /CONTROLLER/ANT2 -> /CONTROLLER/IDD_OL_LV
- J25 pad 40: /CONTROLLER/ANT3 -> /CONTROLLER/TEMP_LV
- J25 pad 5: /CONTROLLER/SCL0_LV -> /CONTROLLER/SCL_PI_LV
- J25 pad 7: /CONTROLLER/TXD1 -> /CONTROLLER/FAULT_LV
- J8 pad 1: Earth -> /FRONTEND/RF_SW1_EN_
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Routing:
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- added copper zone on B.Cu, net /CONTROLLER/FAN+
- added copper zone on B.Cu, net /FRONTEND/RF_SW1
- added copper zone on B.Cu, net /FRONTEND/RF_SW2
- added copper zone on B.Cu, net /FRONTEND/VDD_IN
- added copper zone on In2.Cu, net /FRONTEND/VDD_IN
- added copper zone on F.Cu, net /FRONTEND/VDD_OUT
- added copper zone on In1.Cu, net /FRONTEND/VDD_OUT
- added copper zone on B.Cu, net Net-(C26-Pad1)
- added copper zone on B.Cu, net Net-(C4-Pad1)
- added copper zone on B.Cu, net Net-(C55-Pad2)
- removed copper zone on B.Cu, net /SEQUENCER/VDD
- removed copper zone on F.Cu, net /SEQUENCER/VDD
- removed copper zone on In1.Cu, net /SEQUENCER/VDD
- removed copper zone on In2.Cu, net /SEQUENCER/VDD
- removed copper zone on B.Cu, net /SEQUENCER/VDD_IN
- removed copper zone on F.Cu, net /SEQUENCER/VDD_IN
- removed copper zone on In1.Cu, net /SEQUENCER/VDD_IN
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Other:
- board text added: "13V8"
- board text added: "ALC"
- board text added: "ALC GAIN"
- board text added: "AMP1"
- board text added: "AMP2"
- board text added: "FAN"
- board text added: "FRONT PANEL"
- board text added: "FWD3"
- board text added: "FWD4"
- board text added: "GND"
- board text added: "GPIO"
- board text added: "HSWR1"
- board text added: "HSWR2"
- board text added: "HSWR3"
- board text added: "HSWR4"
- board text added: "I2C"
- board text added: "ICSP"
- board text added: "IDD OL"
- board text added: "MAINS"
- board text added: "POWER"
- board text added: "POWER SUPPLY"
- board text added: "PTT"
- board text added: "REF3"
- board text added: "REF4"
- board text added: "RF OL"
- board text added: "RF SELECT"
- board text added: "RF SWITCH AMP IN"
- board text added: "RF SWITCH AMP OUT"
- board text added: "RPI"
- board text added: "TEMP1"
- board text added: "TEMP2"
- board text added: "UART"
- board text added: "VDD IN"
- board text added: "VDD OUT"

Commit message: RC1
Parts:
- added REF**: Symbol_Attention_CopperTop_Small, Symbol:Symbol_Attention_CopperTop_Small, F.Cu at (47.0, 136.0)
- C65: value 100n -> 10n
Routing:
- net /CONTROLLER/SCL_PI_HV: track 143.2 -> 146.5 mm
- net Net-(R44-Pad1): track 159.6 -> 158.4 mm
- net Net-(D5-Pad2): track 54.9 -> 54.3 mm
- net Earth: vias 50 -> 54
- added copper zone on B.Cu, net Net-(C54-Pad2)
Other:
- board text added: "RS232"
- board text removed: "UART"

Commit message: RC2
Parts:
- added R102: 110, Resistor_SMD:R_0805_2012Metric_Pad1.15x1.40mm_HandSolder, B.Cu at (177.8, 81.2)
- added R77: 110, Resistor_SMD:R_0805_2012Metric_Pad1.15x1.40mm_HandSolder, B.Cu at (119.8, 68.2)
- added R79: 110, Resistor_SMD:R_0805_2012Metric_Pad1.15x1.40mm_HandSolder, B.Cu at (151.2, 68.2)
- C22, C23, C24, C25, C37, C38, C39, C40, C48: value 47n -> 1n
- R30: value 68k -> 47k
- R34: value 100k -> 10k
- R35: value 6k8 -> 680
- R54, R66, R68, R70: value 47k -> 4k7
- R55, R67, R69, R71: value 15k -> 1k
- RV3: value 50k -> 20k
- RV7: renamed from RV6; value 50k -> 20k
- RV8: renamed from RV7; value 50k -> 20k
- RV9: renamed from RV8; value 50k -> 20k
- moved Q17 4.24 mm to (174.0, 81.2)
- moved Q7 4.00 mm to (122.5, 68.2)
- moved Q8 4.00 mm to (154.0, 68.2)
- moved R76 3.25 mm to (117.8, 68.2), turned to 270 degrees
- moved R78 3.25 mm to (149.2, 68.2), turned to 270 degrees
- moved R84 0.75 mm to (113.5, 73.5)
- moved R85 0.75 mm to (145.0, 73.5)
- renumbered C20 to C19, C19 to C20, R98 to R100, R99 to R101, R77 to R78, R78 to R80, R79 to R81, R80 to R82, R81 to R83, R82 to R84, R83 to R85, R84 to R86, R85 to R87, R86 to R88, R87 to R89, R88 to R90, R89 to R91, R90 to R92, R91 to R93, R92 to R94, R93 to R95, R94 to R96, R95 to R97, R96 to R98, R97 to R99, RV9 to RV6, U9 to U10, U10 to U9
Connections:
- Q18 pad 1: Net-(Q17-Pad3) -> Net-(Q18-Pad1)
- Q8 pad 3: Net-(Q10-Pad1) -> Net-(Q8-Pad3)
- Q9 pad 1: Net-(Q7-Pad3) -> Net-(Q9-Pad1)
- R76 pad 1: Net-(Q7-Pad3) -> Net-(Q9-Pad1)
- R97 pad 1: Net-(Q17-Pad3) -> Net-(Q18-Pad1)
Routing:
- net Net-(Q17-Pad1): track 11.6 -> 7.44 mm
- net Net-(Q18-Pad1): track 0.00 -> 4.00 mm
- net Net-(Q9-Pad1): track 0.00 -> 3.93 mm
- net Net-(Q7-Pad3): track 5.86 -> 2.17 mm
- net Net-(Q17-Pad3): track 4.67 -> 1.72 mm
- net Net-(Q8-Pad3): track 0.00 -> 2.17 mm
- net /RF_SW2_EN: track 44.4 -> 46.3 mm
- net Net-(Q10-Pad1): track 5.86 -> 3.93 mm
- net +12V: track 422.1 -> 420.8 mm
- net Earth: vias 54 -> 53
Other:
- board text added: "VDC"
- board text removed: "POWER SUPPLY"

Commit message: RC2
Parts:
- renumbered RV7 to RV6, RV8 to RV7, RV9 to RV8, RV6 to RV9
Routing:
- net /CONTROLLER/ILK: track 43.7 -> 42.9 mm
- net Earth: vias 53 -> 52
